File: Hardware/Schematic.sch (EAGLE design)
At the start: 7 parts, among them J1 SAMACSYS_PARTS_USB4110-GF-A

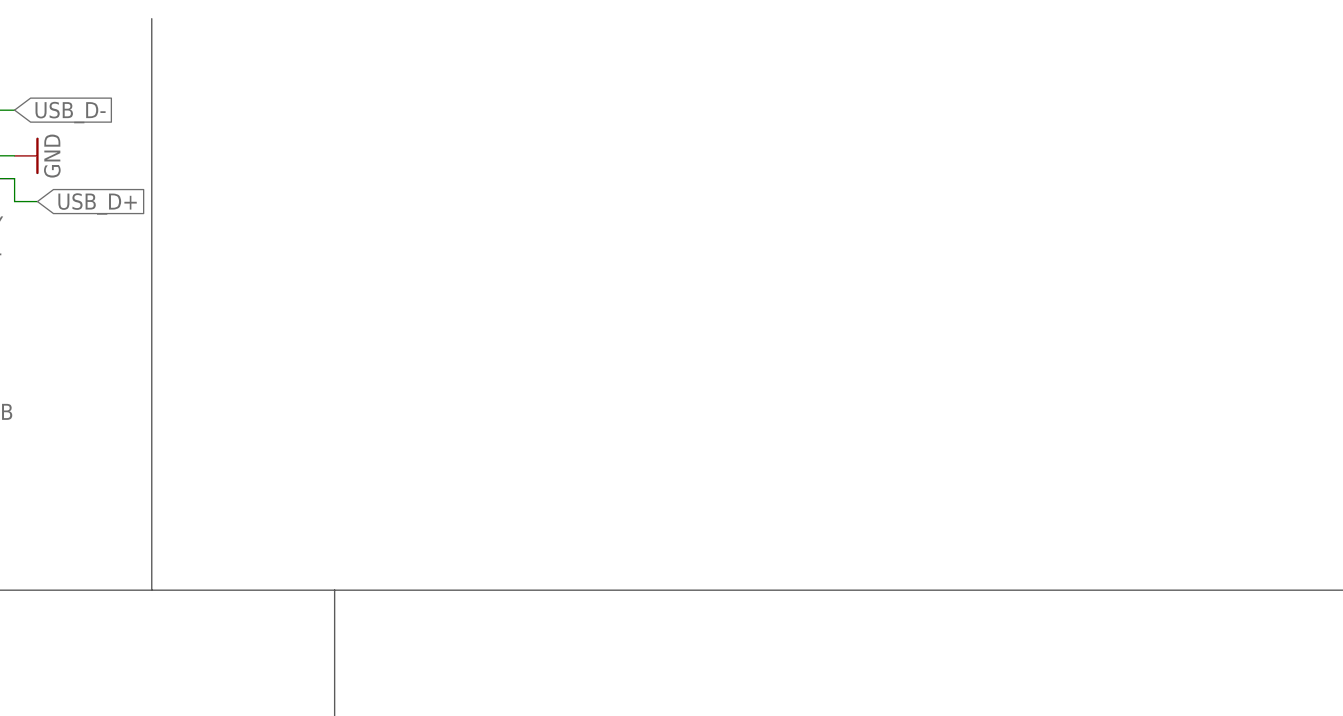
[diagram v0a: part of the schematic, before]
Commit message: add LDO Voltage Regulator
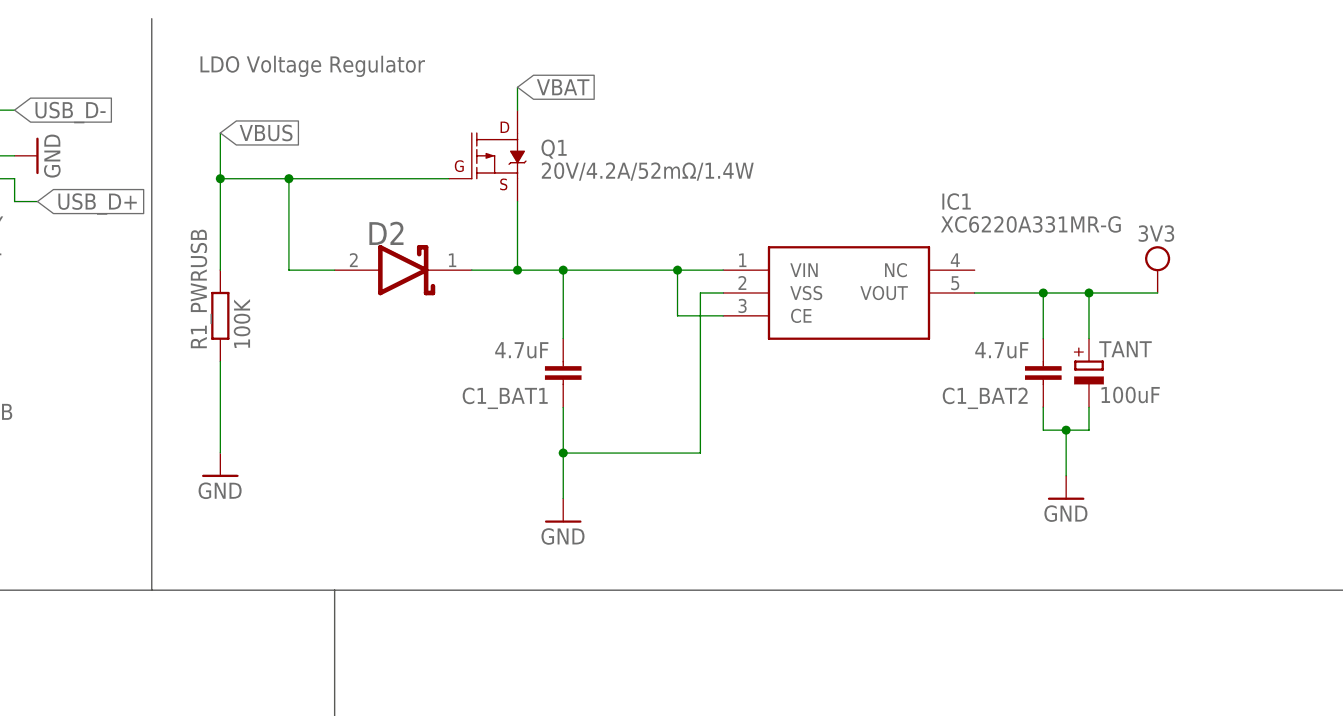
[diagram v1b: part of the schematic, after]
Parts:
- added C1_BAT1, C1_BAT2: 4.7uF, DeskAssistant v19 v1.flbr:ESP32_WROVER_EAGLE-LTSPICE_CC0402
- added D2: ESP32_WROVER_AVX---SD0805S020S1R0_AVX_SD0805S020S1R0_0_0AVX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, DeskAssistant v19 v1.flbr:ESP32_WROVER_AVX---SD0805S020S1R0_AVX_SD0805S020S1R0_0_0AVX_SD0805S020S1R0_0_0
- added IC1: XC6220A331MR-G, DeskAssistant v19 v1.flbr:XC6220A331MR-G
- added Q1: 20V/4.2A/52mΩ/1.4W, DeskAssistant v19 v1.flbr:ESP32_WROVER_SPARKFUN-DISCRETESEMI_MOSFET_PCH-DMG2305UX-7
- added R1_PWRUSB: 100K, DeskAssistant v19 v1.flbr:ESP32_WROVER_EAGLE-LTSPICE_RR0402
- added TANT: 100uF, DeskAssistant v19 v1.flbr:RCL_CPOL-EUCT3528
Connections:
- new net 3V3: C1_BAT2.2, IC1.VOUT, TANT.+
- new net N$3: C1_BAT1.2, D2.CATHODE, IC1.CE, IC1.VIN, Q1.S
- new net VBAT: Q1.D
- net GND: now also C1_BAT1.1, C1_BAT2.1, IC1.VSS, R1_PWRUSB.1, TANT.-
- net VBUS: now also D2.ANODE, Q1.G, R1_PWRUSB.2
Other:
- note added: "LDO Voltage Regulator"
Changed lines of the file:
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@@
 <part name="D1" library="DeskAssistant v19 v1.flbr" library_urn="urn:adsk.wipprod:fs.file:vf.vVvdDOfaSfavM5thX5SjWw" deviceset="USBLC6-2SC6Y" device=""/>
 <part name="GND7" library="DeskAssistant v19 v1.flbr" library_urn="urn:adsk.wipprod:fs.file:vf.vVvdDOfaSfavM5thX5SjWw" deviceset="GND" device=""/>
+<part name="IC1" library="DeskAssistant v19 v1.flbr" library_urn="urn:adsk.wipprod:fs.file:vf.vVvdDOfaSfavM5thX5SjWw" deviceset="XC6220A331MR-G" device=""/>
+<part name="TANT" library="DeskAssistant v19 v1.flbr" library_urn="urn:adsk.wipprod:fs.file:vf.vVvdDOfaSfavM5thX5SjWw" deviceset="RCL_CPOL-EU" device="CT3528" value="100uF"/>
+<part name="SUPPLY1" library="DeskAssistant v19 v1.flbr" library_urn="urn:adsk.wipprod:fs.file:vf.vVvdDOfaSfavM5thX5SjWw" deviceset="3V3-CIRCLE" device="" value="3V3"/>
+<part name="GND8" library="DeskAssistant v19 v1.flbr" library_urn="urn:adsk.wipprod:fs.file:vf.vVvdDOfaSfavM5thX5SjWw" deviceset="GND" device=""/>
+<part name="D2" library="DeskAssistant v19 v1.flbr" library_urn="urn:adsk.wipprod:fs.file:vf.vVvdDOfaSfavM5thX5SjWw" deviceset="ESP32_WROVER_AVX---SD0805S020S1R0_AVX_SD0805S020S1R0_0_0" device="AVX_SD0805S020S1R0_0_0"/>
+<part name="GND9" library="DeskAssistant v19 v1.flbr" library_urn="urn:adsk.wipprod:fs.file:vf.vVvdDOfaSfavM5thX5SjWw" deviceset="GND" device=""/>
+<part name="Q1" library="DeskAssistant v19 v1.flbr" library_urn="urn:adsk.wipprod:fs.file:vf.vVvdDOfaSfavM5thX5SjWw" deviceset="ESP32_WROVER_SPARKFUN-DISCRETESEMI_MOSFET_PCH" device="-DMG2305UX-7" value="20V/4.2A/52mΩ/1.4W"/>
+<part name="R1_PWRUSB" library="DeskAssistant v19 v1.flbr" library_urn="urn:adsk.wipprod:fs.file:vf.vVvdDOfaSfavM5thX5SjWw" deviceset="ESP32_WROVER_EAGLE-LTSPICE_R" device="R0402" value="100K"/>
+<part name="GND10" library="DeskAssistant v19 v1.flbr" library_urn="urn:adsk.wipprod:fs.file:vf.vVvdDOfaSfavM5thX5SjWw" deviceset="GND" device=""/>
+<part name="C1_BAT2" library="DeskAssistant v19 v1.flbr" library_urn="urn:adsk.wipprod:fs.file:vf.vVvdDOfaSfavM5thX5SjWw" deviceset="ESP32_WROVER_EAGLE-LTSPICE_C" device="C0402" value="4.7uF"/>
+<part name="C1_BAT1" library="DeskAssistant v19 v1.flbr" library_urn="urn:adsk.wipprod:fs.file:vf.vVvdDOfaSfavM5thX5SjWw" deviceset="ESP32_WROVER_EAGLE-LTSPICE_C" device="C0402" value="4.7uF"/>
 </parts>
 <sheets>
@@
 <text x="-157.48" y="269.24" size="1.778" layer="97">USB C connector &amp;
 ESD Protection</text>
+<text x="-2.54" y="271.78" size="1.778" layer="95" align="center">LDO Voltage Regulator</text>
 </plain>
 <instances>
@@
 <instance part="GND7" gate="1" x="-33.02" y="261.62" smashed="yes" rot="R90">
 <attribute name="VALUE" x="-30.48" y="259.08" size="1.778" layer="96" rot="R90"/>
+</instance>
+<instance part="IC1" gate="G$1" x="43.18" y="248.92" smashed="yes">
+<attribute name="NAME" x="67.31" y="256.54" size="1.778" layer="95" align="center-left"/>
+<attribute name="VALUE" x="67.31" y="254" size="1.778" layer="96" align="center-left"/>
+</instance>
+<instance part="TANT" gate="G$1" x="83.82" y="238.76" smashed="yes">
+<attribute name="NAME" x="84.963" y="239.2426" size="1.778" layer="95"/>
+<attribute name="VALUE" x="84.963" y="234.1626" size="1.778" layer="96"/>
+</instance>
+<instance part="SUPPLY1" gate="G$1" x="91.44" y="248.92" smashed="yes">
+<attribute name="VALUE" x="91.313" y="252.095" size="1.778" layer="96" align="bottom-center"/>
+</instance>
+<instance part="GND8" gate="1" x="81.28" y="223.52" smashed="yes">
+<attribute name="VALUE" x="78.74" y="220.98" size="1.778" layer="96"/>
+</instance>
+<instance part="D2" gate="G$0" x="2.54" y="254" smashed="yes">
+<attribute name="NAME" x="3.556" y="254.254" size="2.54" layer="95" align="top-left"/>
+</instance>
+<instance part="GND9" gate="1" x="25.4" y="220.98" smashed="yes">
+<attribute name="VALUE" x="22.86" y="218.44" size="1.778" layer="96"/>
+</instance>
+<instance part="Q1" gate="G$1" x="17.78" y="261.62" smashed="yes">
+<attribute name="NAME" x="22.86" y="261.62" size="1.778" layer="95" font="vector"/>
+<attribute name="VALUE" x="22.86" y="259.08" size="1.778" layer="96" font="vector"/>
+</instance>
+<instance part="R1_PWRUSB" gate="G$1" x="-12.7" y="243.84" smashed="yes" rot="R90">
+<attribute name="NAME" x="-14.1986" y="240.03" size="1.778" layer="95" rot="R90"/>
+<attribute name="VALUE" x="-9.398" y="240.03" size="1.778" layer="96" rot="R90"/>
+<attribute name="NAME" x="-14.1986" y="240.03" size="1.778" layer="95" rot="R90"/>
+<attribute name="VALUE" x="-9.398" y="240.03" size="1.778" layer="96" rot="R90"/>
+</instance>
+<instance part="GND10" gate="1" x="-12.7" y="226.06" smashed="yes">
+<attribute name="VALUE" x="-15.24" y="223.52" size="1.778" layer="96"/>
+</instance>
+<instance part="C1_BAT2" gate="G$1" x="78.74" y="236.22" smashed="yes" rot="R180">
+<attribute name="NAME" x="77.216" y="235.839" size="1.778" layer="95" rot="R180"/>
+<attribute name="VALUE" x="77.216" y="240.919" size="1.778" layer="96" rot="R180"/>
+</instance>
+<instance part="C1_BAT1" gate="G$1" x="25.4" y="236.22" smashed="yes" rot="R180">
+<attribute name="NAME" x="23.876" y="235.839" size="1.778" layer="95" rot="R180"/>
+<attribute name="VALUE" x="23.876" y="240.919" size="1.778" layer="96" rot="R180"/>
 </instance>
 </instances>
@@
 <pinref part="GND7" gate="1" pin="GND"/>
 </segment>
+<segment>
+<pinref part="TANT" gate="G$1" pin="-"/>
+<wire x1="83.82" y1="233.68" x2="83.82" y2="231.14" width="0.1524" layer="91"/>
+<wire x1="83.82" y1="231.14" x2="81.28" y2="231.14" width="0.1524" layer="91"/>
+<wire x1="81.28" y1="231.14" x2="81.28" y2="226.06" width="0.1524" layer="91"/>
+<pinref part="GND8" gate="1" pin="GND"/>
+<wire x1="78.74" y1="233.68" x2="78.74" y2="231.14" width="0.1524" layer="91"/>
+<wire x1="78.74" y1="231.14" x2="81.28" y2="231.14" width="0.1524" layer="91"/>
+<junction x="81.28" y="231.14"/>
+<pinref part="C1_BAT2" gate="G$1" pin="1"/>
+</segment>
+<segment>
+<wire x1="25.4" y1="223.52" x2="25.4" y2="228.6" width="0.1524" layer="91"/>
+<wire x1="25.4" y1="228.6" x2="40.64" y2="228.6" width="0.1524" layer="91"/>
+<wire x1="40.64" y1="228.6" x2="40.64" y2="246.38" width="0.1524" layer="91"/>
+<wire x1="40.64" y1="246.38" x2="43.18" y2="246.38" width="0.1524" layer="91"/>
+<pinref part="IC1" gate="G$1" pin="VSS"/>
+<pinref part="GND9" gate="1" pin="GND"/>
+<wire x1="25.4" y1="228.6" x2="25.4" y2="233.68" width="0.1524" layer="91"/>
+<junction x="25.4" y="228.6"/>
+<pinref part="C1_BAT1" gate="G$1" pin="1"/>
+</segment>
+<segment>
+<wire x1="-12.7" y1="228.6" x2="-12.7" y2="238.76" width="0.1524" layer="91"/>
+<pinref part="R1_PWRUSB" gate="G$1" pin="1"/>
+<pinref part="GND10" gate="1" pin="GND"/>
+</segment>
 </net>
 <net name="VUSB" class="0">
@@
 <wire x1="-76.2" y1="261.62" x2="-71.12" y2="261.62" width="0.1524" layer="91"/>
 </segment>
+<segment>
+<pinref part="Q1" gate="G$1" pin="G"/>
+<wire x1="12.7" y1="259.08" x2="-5.08" y2="259.08" width="0.1524" layer="91"/>
+<wire x1="-5.08" y1="259.08" x2="-5.08" y2="248.92" width="0.1524" layer="91"/>
+<wire x1="-5.08" y1="248.92" x2="0" y2="248.92" width="0.1524" layer="91"/>
+<pinref part="D2" gate="G$0" pin="ANODE"/>
+<wire x1="-5.08" y1="259.08" x2="-12.7" y2="259.08" width="0.1524" layer="91"/>
+<junction x="-5.08" y="259.08"/>
+<label x="-12.7" y="264.16" size="1.778" layer="95" xref="yes"/>
+<wire x1="-12.7" y1="264.16" x2="-12.7" y2="259.08" width="0.1524" layer="91"/>
+<wire x1="-12.7" y1="259.08" x2="-12.7" y2="248.92" width="0.1524" layer="91"/>
+<junction x="-12.7" y="259.08"/>
+<pinref part="R1_PWRUSB" gate="G$1" pin="2"/>
+</segment>
 </net>
 <net name="N$1" class="0">
@@
 </segment>
 </net>
+<net name="3V3" class="0">
+<segment>
+<pinref part="IC1" gate="G$1" pin="VOUT"/>
+<wire x1="71.12" y1="246.38" x2="78.74" y2="246.38" width="0.1524" layer="91"/>
+<wire x1="78.74" y1="246.38" x2="83.82" y2="246.38" width="0.1524" layer="91"/>
+<wire x1="83.82" y1="246.38" x2="91.44" y2="246.38" width="0.1524" layer="91"/>
+<pinref part="SUPPLY1" gate="G$1" pin="3V3"/>
+<pinref part="TANT" gate="G$1" pin="+"/>
+<wire x1="83.82" y1="241.3" x2="83.82" y2="246.38" width="0.1524" layer="91"/>
+<junction x="83.82" y="246.38"/>
+<junction x="78.74" y="246.38"/>
+<wire x1="78.74" y1="246.38" x2="78.74" y2="241.3" width="0.1524" layer="91"/>
+<pinref part="C1_BAT2" gate="G$1" pin="2"/>
+</segment>
+</net>
+<net name="N$3" class="0">
+<segment>
+<pinref part="D2" gate="G$0" pin="CATHODE"/>
+<wire x1="15.24" y1="248.92" x2="20.32" y2="248.92" width="0.1524" layer="91"/>
+<pinref part="IC1" gate="G$1" pin="VIN"/>
+<wire x1="20.32" y1="248.92" x2="25.4" y2="248.92" width="0.1524" layer="91"/>
+<wire x1="25.4" y1="248.92" x2="38.1" y2="248.92" width="0.1524" layer="91"/>
+<wire x1="38.1" y1="248.92" x2="43.18" y2="248.92" width="0.1524" layer="91"/>
+<pinref part="IC1" gate="G$1" pin="CE"/>
+<wire x1="43.18" y1="243.84" x2="38.1" y2="243.84" width="0.1524" layer="91"/>
+<wire x1="38.1" y1="243.84" x2="38.1" y2="248.92" width="0.1524" layer="91"/>
+<junction x="38.1" y="248.92"/>
+<pinref part="Q1" gate="G$1" pin="S"/>
+<wire x1="20.32" y1="256.54" x2="20.32" y2="248.92" width="0.1524" layer="91"/>
+<junction x="20.32" y="248.92"/>
+<junction x="25.4" y="248.92"/>
+<wire x1="25.4" y1="248.92" x2="25.4" y2="241.3" width="0.1524" layer="91"/>
+<pinref part="C1_BAT1" gate="G$1" pin="2"/>
+</segment>
+</net>
+<net name="VBAT" class="0">
+<segment>
+<pinref part="Q1" gate="G$1" pin="D"/>
+<wire x1="20.32" y1="266.7" x2="20.32" y2="269.24" width="0.1524" layer="91"/>
+<label x="20.32" y="269.24" size="1.778" layer="95" xref="yes"/>
+</segment>
+</net>
